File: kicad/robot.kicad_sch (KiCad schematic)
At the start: 27 parts, among them J1 Accelerometer, M1 Motor_DC, M2 Motor_DC, M3 Motor_DC, M4 Motor_DC, Q1 NMOS, SW1 SW_Push_45deg, SW2 SW_Push_45deg, U1 LT1963AxQ-3.3, U2 ESP32-WROOM-32, U3 DRV8833PW, U4 DRV8833PW, U5 MAX1811, U7 L7806

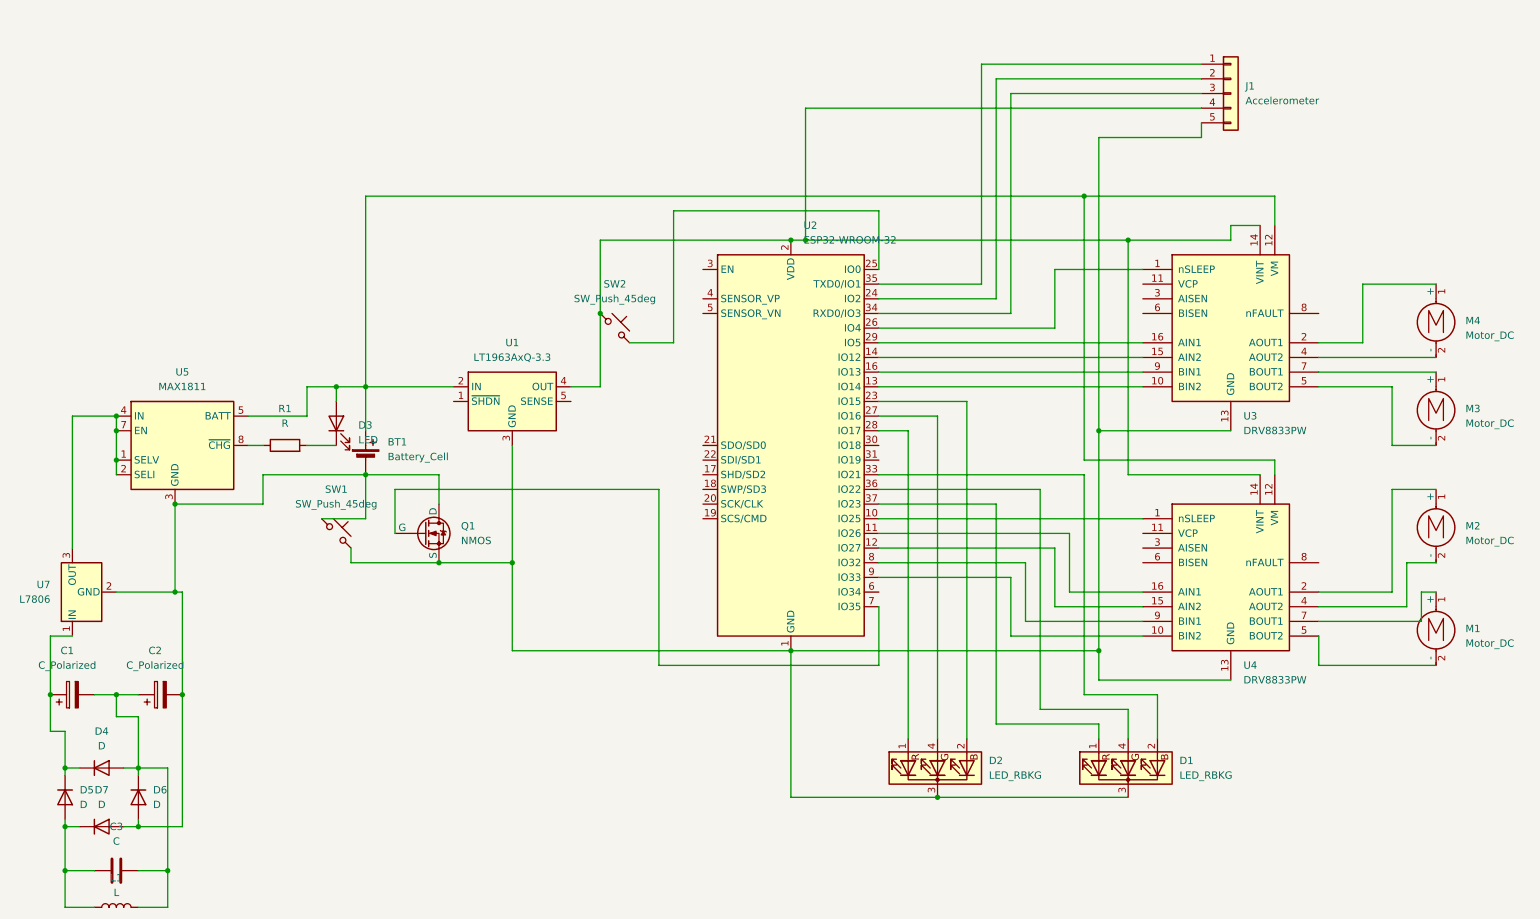
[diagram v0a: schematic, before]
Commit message: Add SymFoots
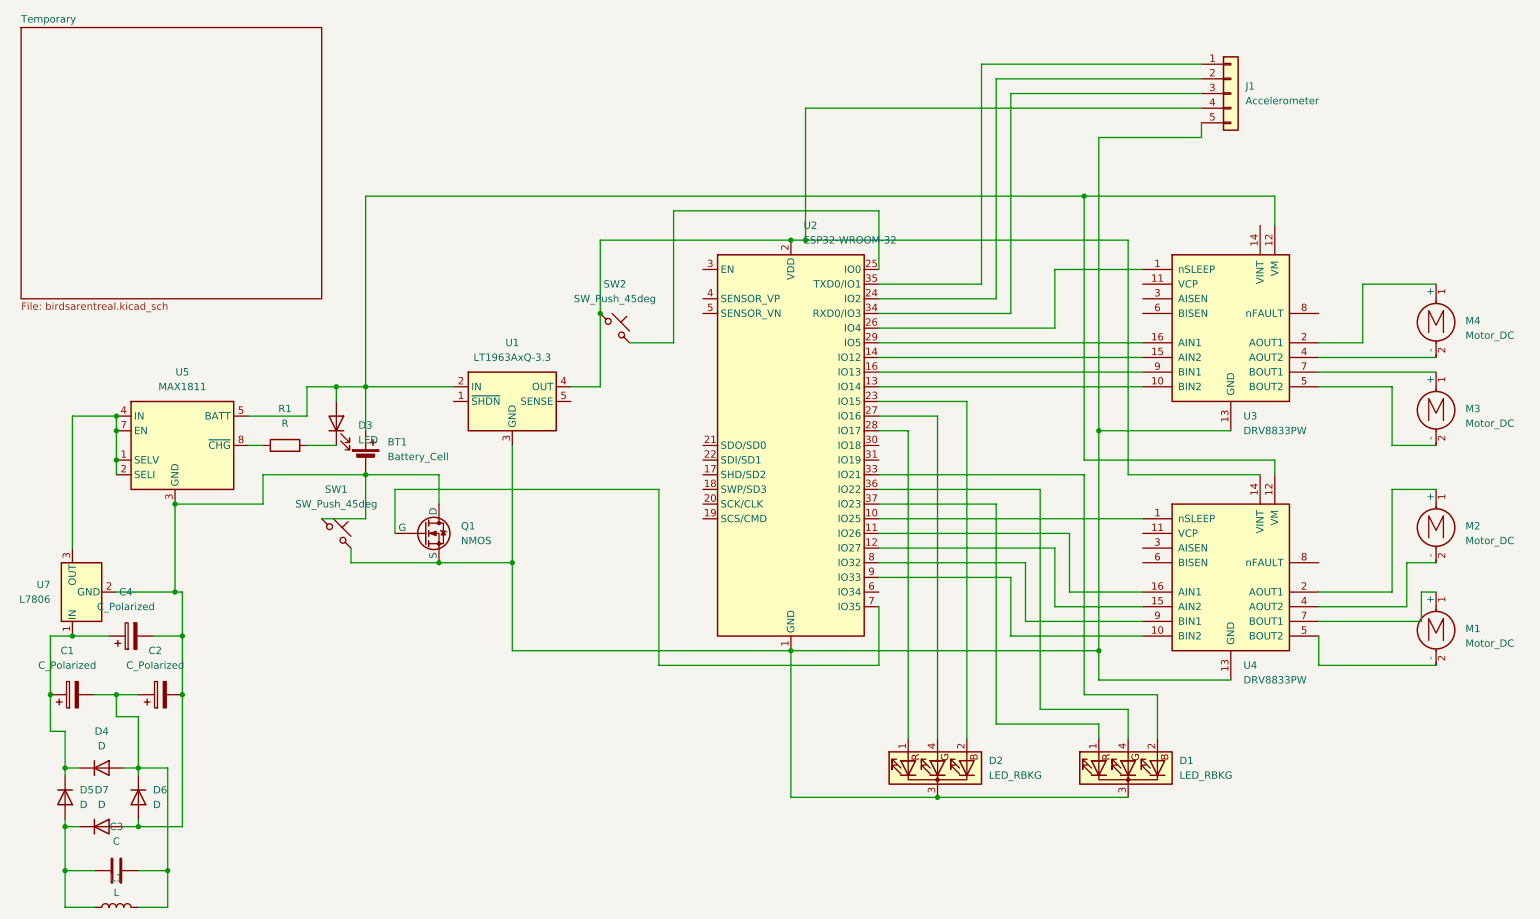
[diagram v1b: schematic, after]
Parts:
- added C4: C_Polarized, symbol Device:C_Polarized
- D2: footprint (none) -> Connector_PinHeader_1.00mm:PinHeader_1x04_P1.00mm_Vertical
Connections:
- net at BT1.2 (-), C2.2, D6.2 (A)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: now also C4.2
- net at C1.1, D4.1 (K), D5.1 (K)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: now also C4.1
- net at J1.4 (Pin_4), SW2.1, U1.4 (OUT)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: no longer U3.14 (VINT)
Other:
- added sheet Temporary (birdsarentreal.kicad_sch)
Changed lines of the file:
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@@
   (junction (at 40.64 96.52) (diameter 0) (color 0 0 0 0)
   )
+  (junction (at 52.07 127) (diameter 0) (color 0 0 0 0)
+  )
   (junction (at 40.64 91.44) (diameter 0) (color 0 0 0 0)
   )
@@
   (junction (at 182.88 154.94) (diameter 0) (color 0 0 0 0)
   )
-  (junction (at 215.9 58.42) (diameter 0) (color 0 0 0 0)
+  (junction (at 33.02 127) (diameter 0) (color 0 0 0 0)
   )
   (junction (at 44.45 160.02) (diameter 0) (color 0 0 0 0)
@@
     (stroke (width 0) (type default))
   )
+  (wire (pts (xy 46.99 127) (xy 52.07 127))
+    (stroke (width 0) (type default))
+  )
   (wire (pts (xy 81.28 111.76) (xy 81.28 114.3))
     (stroke (width 0) (type default))
@@
     (stroke (width 0) (type default))
   )
-  (wire (pts (xy 215.9 58.42) (xy 233.68 58.42))
+  (wire (pts (xy 33.02 127) (xy 39.37 127))
     (stroke (width 0) (type default))
   )
@@
     (stroke (width 0) (type default))
   )
-  (wire (pts (xy 52.07 137.16) (xy 52.07 119.38))
-    (stroke (width 0) (type default))
-  )
-  (wire (pts (xy 233.68 58.42) (xy 233.68 55.88))
+  (wire (pts (xy 52.07 137.16) (xy 52.07 127))
     (stroke (width 0) (type default))
   )
@@
     (stroke (width 0) (type default))
   )
-  (wire (pts (xy 233.68 55.88) (xy 238.76 55.88))
-    (stroke (width 0) (type default))
-  )
   (wire (pts (xy 76.2 106.68) (xy 83.82 106.68))
     (stroke (width 0) (type default))
@@
   )
   (wire (pts (xy 63.5 88.9) (xy 73.66 88.9))
+    (stroke (width 0) (type default))
+  )
+  (wire (pts (xy 52.07 127) (xy 52.07 119.38))
     (stroke (width 0) (type default))
   )
@@
     )
   )
+  (symbol (lib_id "Device:C_Polarized") (at 43.18 127 90) (unit 1)
+    (in_bom yes) (on_board yes) (dnp no) (fields_autoplaced)
+    (property "Reference" "C4" (at 42.291 119.38 90)
+      (effects (font (size 1.27 1.27)))
+    )
+    (property "Value" "C_Polarized" (at 42.291 121.92 90)
+      (effects (font (size 1.27 1.27)))
+    )
+    (property "Footprint" "" (at 46.99 126.0348 0)
+      (effects (font (size 1.27 1.27)) hide)
+    )
+    (property "Datasheet" "~" (at 43.18 127 0)
+      (effects (font (size 1.27 1.27)) hide)
+    )
+    (pin "1")
+    (pin "2")
+    (instances
+      (project "robot"
+        (path "/9f6eb88e-d254-4b8d-b64f-838940a89234"
+          (reference "C4") (unit 1)
+        )
+      )
+    )
+  )
   (symbol (lib_id "Switch:SW_Push_45deg") (at 127 73.66 0) (unit 1)
     (in_bom yes) (on_board yes) (dnp no) (fields_autoplaced)
@@
       (effects (font (size 1.27 1.27)) (justify right))
     )
-    (property "Footprint" "" (at 184.15 149.86 0)
+    (property "Footprint" "Connector_PinHeader_1.00mm:PinHeader_1x04_P1.00mm_Vertical" (at 184.15 149.86 0)
       (effects (font (size 1.27 1.27)) hide)
     )
@@
       )
     )
+  )
+  (sheet (at 24.13 21.59) (size 52.07 46.99) (fields_autoplaced)
+    (stroke (width 0.1524) (type solid))
+    (fill (color 0 0 0 0.0000))
+    (property "Sheetname" "Temporary" (at 24.13 20.8784 0)
+      (effects (font (size 1.27 1.27)) (justify left bottom))
+    )
+    (property "Sheetfile" "birdsarentreal.kicad_sch" (at 24.13 69.1646 0)
+      (effects (font (size 1.27 1.27)) (justify left top))
+    )
+    (instances
+      (project "robot"
+        (path "/9f6eb88e-d254-4b8d-b64f-838940a89234" (page "2"))
+      )
+    )

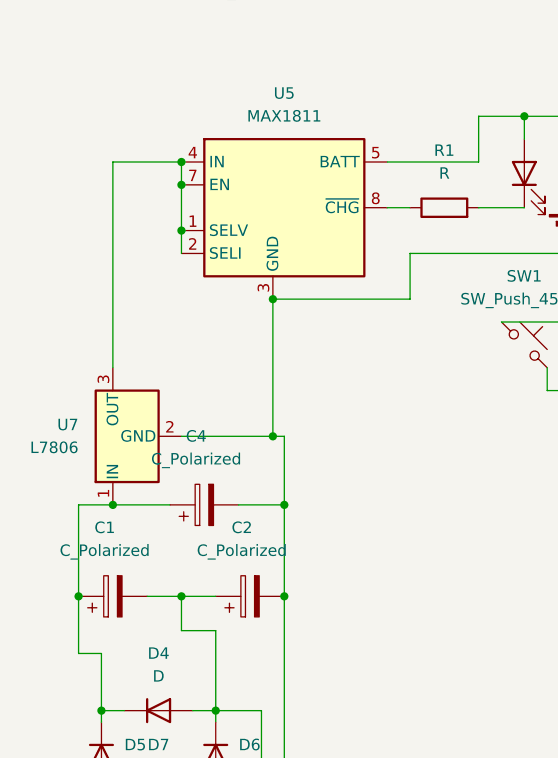
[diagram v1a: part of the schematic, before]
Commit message: Add all symbols and values
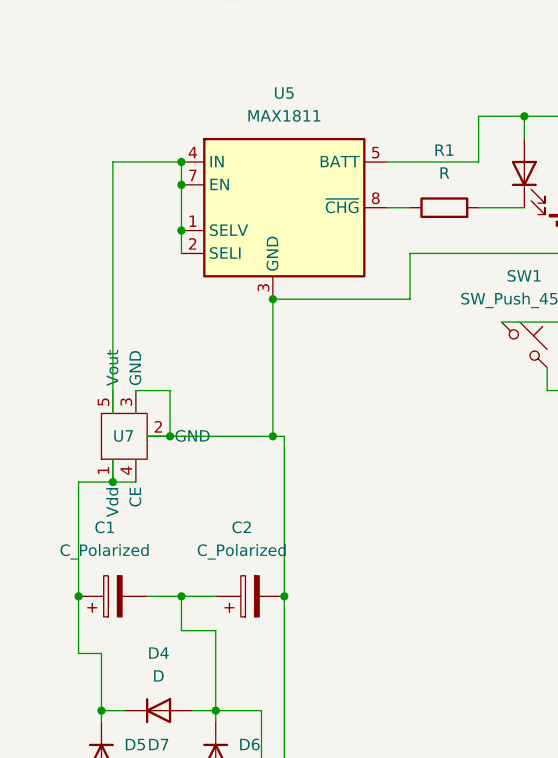
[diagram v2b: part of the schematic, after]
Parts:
- removed C4: C_Polarized, symbol Device:C_Polarized
- removed U7: L7806, symbol Regulator_Linear:L7806
- added U7: ~, Package_TO_SOT_SMD:SOT-89-5, symbol R1500H050B:R1500H050B
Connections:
- net at BT1.2 (-), C2.2, D6.2 (A)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: now also U7.2 (GND), U7.3 (GND)
- net at C1.1, D4.1 (K), D5.1 (K): now also U7.1 (Vdd), U7.4 (CE)
- net at U5.1 (SELV), U5.2 (SELI), U5.4 (IN)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: now also U7.5 (Vout)
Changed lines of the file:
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@@
   (junction (at 210.82 91.44) (diameter 0) (color 0 0 0 0)
   )
+  (junction (at 33.02 124.46) (diameter 0) (color 0 0 0 0)
+  )
   (junction (at 52.07 137.16) (diameter 0) (color 0 0 0 0)
   )
@@
   (junction (at 40.64 96.52) (diameter 0) (color 0 0 0 0)
   )
-  (junction (at 52.07 127) (diameter 0) (color 0 0 0 0)
-  )
   (junction (at 40.64 91.44) (diameter 0) (color 0 0 0 0)
   )
@@
   (junction (at 182.88 154.94) (diameter 0) (color 0 0 0 0)
   )
-  (junction (at 33.02 127) (diameter 0) (color 0 0 0 0)
-  )
   (junction (at 44.45 160.02) (diameter 0) (color 0 0 0 0)
   )
@@
   (junction (at 157.48 58.42) (diameter 0) (color 0 0 0 0)
   )
+  (junction (at 39.37 119.38) (diameter 0) (color 0 0 0 0)
+  )
   (junction (at 96.52 114.3) (diameter 0) (color 0 0 0 0)
   )
@@
     (stroke (width 0) (type default))
   )
+  (wire (pts (xy 35.56 121.92) (xy 35.56 124.46))
+    (stroke (width 0) (type default))
+  )
+  (wire (pts (xy 35.56 124.46) (xy 33.02 124.46))
+    (stroke (width 0) (type default))
+  )
   (wire (pts (xy 44.45 140.97) (xy 40.64 140.97))
     (stroke (width 0) (type default))
@@
     (stroke (width 0) (type default))
   )
+  (wire (pts (xy 36.83 119.38) (xy 39.37 119.38))
+    (stroke (width 0) (type default))
+  )
   (wire (pts (xy 83.82 99.06) (xy 83.82 106.68))
     (stroke (width 0) (type default))
@@
     (stroke (width 0) (type default))
   )
-  (wire (pts (xy 46.99 127) (xy 52.07 127))
-    (stroke (width 0) (type default))
-  )
   (wire (pts (xy 81.28 111.76) (xy 81.28 114.3))
     (stroke (width 0) (type default))
@@
     (stroke (width 0) (type default))
   )
-  (wire (pts (xy 29.21 137.16) (xy 29.21 127))
+  (wire (pts (xy 29.21 137.16) (xy 29.21 124.46))
     (stroke (width 0) (type default))
   )
@@
     (stroke (width 0) (type default))
   )
-  (wire (pts (xy 40.64 119.38) (xy 50.8 119.38))
-    (stroke (width 0) (type default))
-  )
   (wire (pts (xy 241.3 50.8) (xy 241.3 55.88))
     (stroke (width 0) (type default))
   )
+  (wire (pts (xy 33.02 121.92) (xy 33.02 124.46))
+    (stroke (width 0) (type default))
+  )
   (wire (pts (xy 215.9 139.7) (xy 200.66 139.7))
     (stroke (width 0) (type default))
@@
     (stroke (width 0) (type default))
   )
+  (wire (pts (xy 35.56 114.3) (xy 39.37 114.3))
+    (stroke (width 0) (type default))
+  )
   (wire (pts (xy 215.9 144.78) (xy 215.9 139.7))
     (stroke (width 0) (type default))
@@
     (stroke (width 0) (type default))
   )
-  (wire (pts (xy 33.02 127) (xy 39.37 127))
-    (stroke (width 0) (type default))
-  )
   (wire (pts (xy 215.9 58.42) (xy 215.9 99.06))
     (stroke (width 0) (type default))
   )
-  (wire (pts (xy 33.02 111.76) (xy 33.02 88.9))
+  (wire (pts (xy 33.02 88.9) (xy 33.02 116.84))
     (stroke (width 0) (type default))
   )
@@
     (stroke (width 0) (type default))
   )
+  (wire (pts (xy 39.37 119.38) (xy 50.8 119.38))
+    (stroke (width 0) (type default))
+  )
   (wire (pts (xy 36.83 137.16) (xy 40.64 137.16))
     (stroke (width 0) (type default))
@@
     (stroke (width 0) (type default))
   )
-  (wire (pts (xy 52.07 137.16) (xy 52.07 127))
+  (wire (pts (xy 52.07 119.38) (xy 52.07 137.16))
     (stroke (width 0) (type default))
   )
@@
     (stroke (width 0) (type default))
   )
+  (wire (pts (xy 29.21 124.46) (xy 33.02 124.46))
+    (stroke (width 0) (type default))
+  )
   (wire (pts (xy 157.48 154.94) (xy 157.48 129.54))
     (stroke (width 0) (type default))
@@
     (stroke (width 0) (type default))
   )
+  (wire (pts (xy 39.37 114.3) (xy 39.37 119.38))
+    (stroke (width 0) (type default))
+  )
   (wire (pts (xy 208.28 96.52) (xy 241.3 96.52))
     (stroke (width 0) (type default))
@@
     (stroke (width 0) (type default))
   )
-  (wire (pts (xy 29.21 127) (xy 33.02 127))
-    (stroke (width 0) (type default))
-  )
   (wire (pts (xy 160.02 35.56) (xy 228.6 35.56))
     (stroke (width 0) (type default))
@@
     (stroke (width 0) (type default))
   )
+  (wire (pts (xy 35.56 114.3) (xy 35.56 116.84))
+    (stroke (width 0) (type default))
+  )
   (wire (pts (xy 241.3 96.52) (xy 241.3 99.06))
     (stroke (width 0) (type default))
@@
   )
   (wire (pts (xy 63.5 88.9) (xy 73.66 88.9))
-    (stroke (width 0) (type default))
-  )
-  (wire (pts (xy 52.07 127) (xy 52.07 119.38))
     (stroke (width 0) (type default))
   )
@@
     )
   )
-  (symbol (lib_id "Regulator_Linear:L7806") (at 33.02 119.38 90) (unit 1)
-    (in_bom yes) (on_board yes) (dnp no) (fields_autoplaced)
-    (property "Reference" "U7" (at 29.21 118.11 90)
-      (effects (font (size 1.27 1.27)) (justify left))
-    )
-    (property "Value" "L7806" (at 29.21 120.65 90)
-      (effects (font (size 1.27 1.27)) (justify left))
-    )
-    (property "Footprint" "" (at 36.83 118.745 0)
-      (effects (font (size 1.27 1.27) italic) (justify left) hide)
-    )
-    (property "Datasheet" "http://www.st.com/content/ccc/resource/technical/document/datasheet/41/4f/b3/b0/12/d4/47/88/CD00000444.pdf/files/CD00000444.pdf/jcr:content/translations/en.CD00000444.pdf" (at 34.29 119.38 0)
+  (symbol (lib_id "R1500H050B:R1500H050B") (at 34.29 119.38 90) (unit 1)
+    (in_bom yes) (on_board yes) (dnp no)
+    (property "Reference" "U7" (at 33.02 119.38 90)
+      (effects (font (size 1.27 1.27)) (justify right))
+    )
+    (property "Value" "~" (at 34.29 119.38 0)
+      (effects (font (size 1.27 1.27)))
+    )
+    (property "Footprint" "Package_TO_SOT_SMD:SOT-89-5" (at 34.29 119.38 0)
+      (effects (font (size 1.27 1.27)) hide)
+    )
+    (property "Datasheet" "" (at 34.29 119.38 0)
       (effects (font (size 1.27 1.27)) hide)
     )
@@
     (pin "2")
     (pin "3")
+    (pin "4")
+    (pin "5")
     (instances
       (project "robot"
@@
         )
       )
-    )
-  )
-  (symbol (lib_id "Device:C_Polarized") (at 43.18 127 90) (unit 1)
-    (in_bom yes) (on_board yes) (dnp no) (fields_autoplaced)
-    (property "Reference" "C4" (at 42.291 119.38 90)
-      (effects (font (size 1.27 1.27)))
-    )
-    (property "Value" "C_Polarized" (at 42.291 121.92 90)
-      (effects (font (size 1.27 1.27)))
-    )
-    (property "Footprint" "" (at 46.99 126.0348 0)
-      (effects (font (size 1.27 1.27)) hide)
-    )
-    (property "Datasheet" "~" (at 43.18 127 0)
-      (effects (font (size 1.27 1.27)) hide)
-    )
-    (pin "1")
-    (pin "2")
-    (instances
-      (project "robot"
-        (path "/9f6eb88e-d254-4b8d-b64f-838940a89234"
-          (reference "C4") (unit 1)
-        )
-      )
